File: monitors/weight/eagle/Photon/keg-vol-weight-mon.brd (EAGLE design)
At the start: 90.5 x 49.9 mm, 18 parts

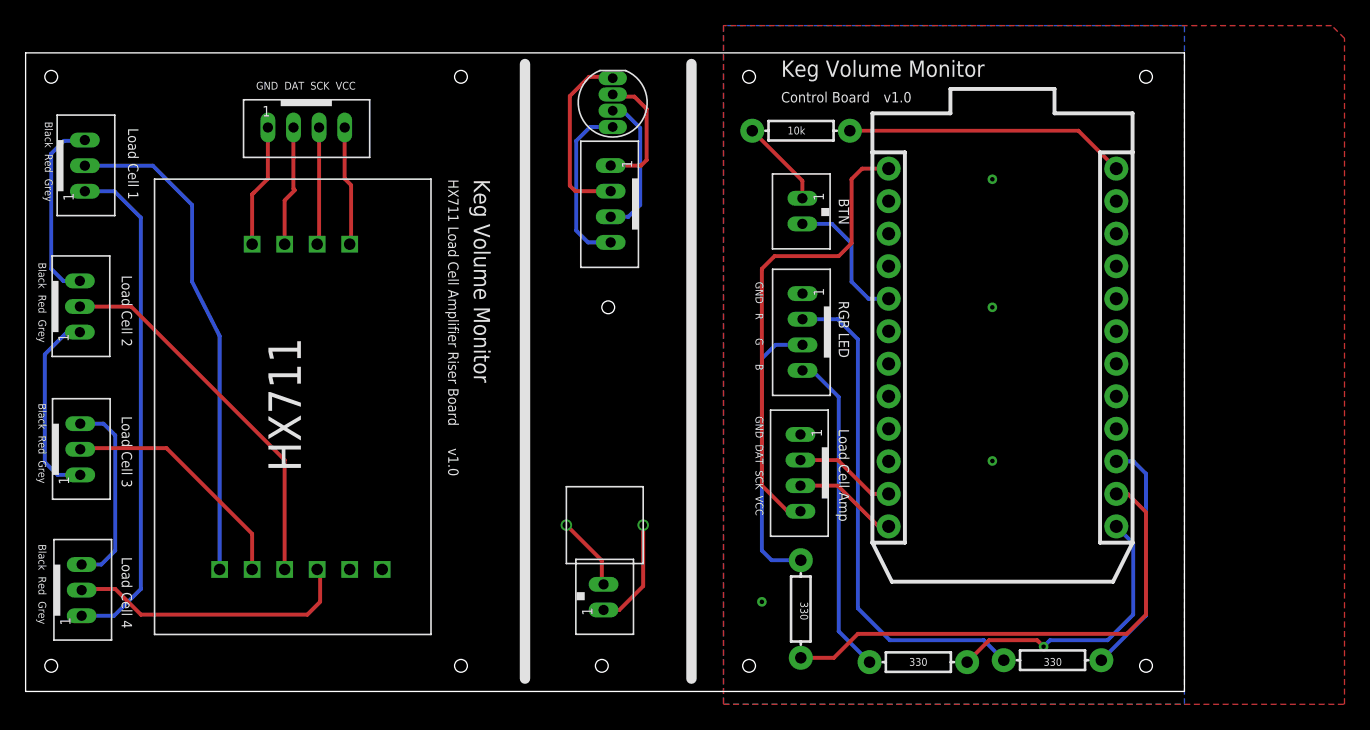
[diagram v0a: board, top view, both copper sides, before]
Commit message: Got the device registration process working
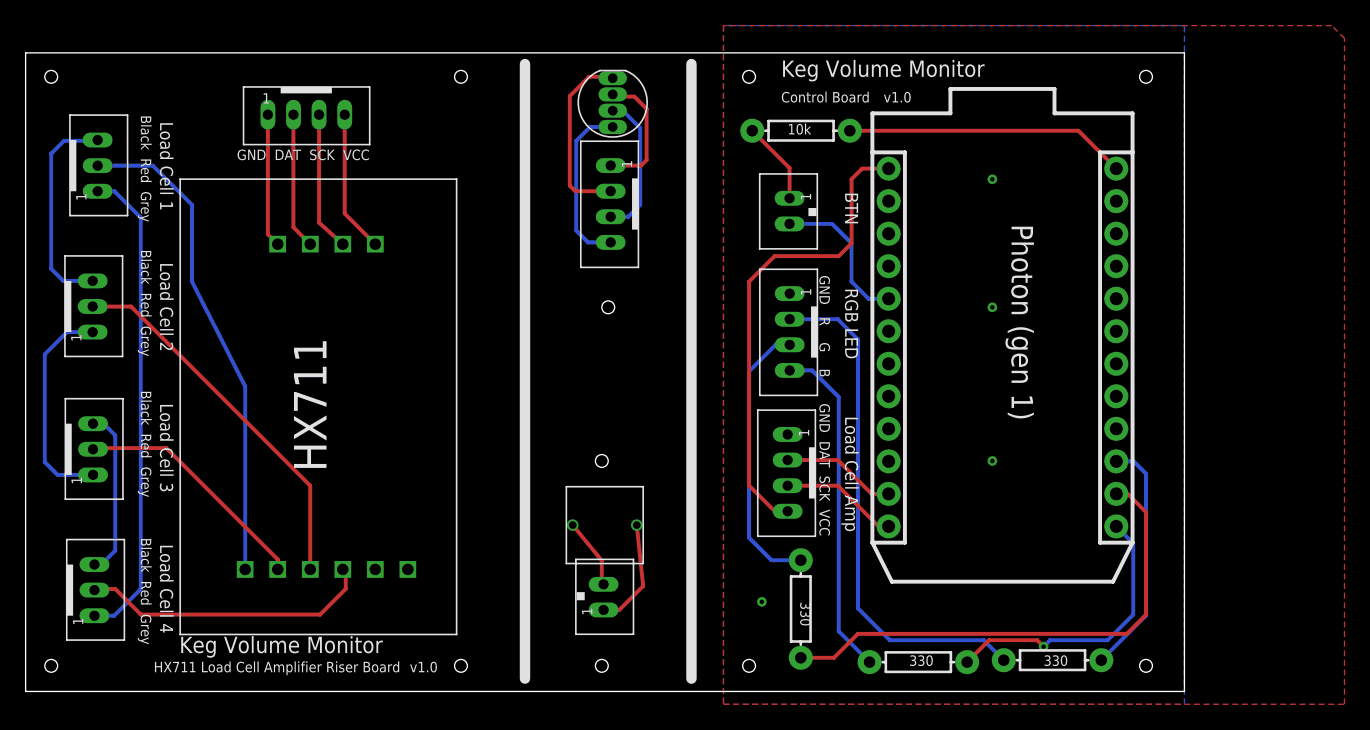
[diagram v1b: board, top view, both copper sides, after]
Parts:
- R1, R2, R3: value 330 -> (none)
- R4: value 10k -> (none)
- moved U$4 2.00 mm to (33.7, 4.45)
- moved U$10 1.00 mm to (5.33, 7.94)
- moved U$2 1.00 mm to (59.7, 37.4)
- moved U$3 1.00 mm to (59.7, 28.1)
- moved U$5 1.00 mm to (59.6, 17.1)
- moved U$6 1.00 mm to (21.9, 45.1)
- moved U$7 1.00 mm to (5.58, 41.1)
- moved U$8 1.00 mm to (5.19, 30.1)
- moved U$9 1.00 mm to (5.22, 18.9)
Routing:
- net N$15: track 39.7 -> 37.7 mm
- net N$14: track 15.2 -> 13.2 mm
- net N$13: track 15.1 -> 17.1 mm
- net N$12: track 14.7 -> 16.7 mm
- net N$18: track 9.18 -> 10.9 mm
- net N$19: track 9.37 -> 11.1 mm
- net N$17: track 9.48 -> 10.7 mm
- net SCK: track 8.20 -> 9.20 mm
- net N$6: track 39.0 -> 40.0 mm
- net N$2: track 25.4 -> 26.4 mm
- net BTN: track 10.9 -> 11.9 mm
- net DT: track 7.98 -> 8.98 mm
- net N$16: track 9.62 -> 10.4 mm
- net N$5: track 38.6 -> 38.1 mm
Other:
- board text added: "Photon (gen 1)"
